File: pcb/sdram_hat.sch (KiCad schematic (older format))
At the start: 25 parts, among them J1 CONN_02X20, J2 CONN_02X20, J3 CONN_02X20, J4 CONN_02X20, J5 JACK_2P

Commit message: Some additional layout work on PCB
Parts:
- J1: footprint Pin_Headers:Pin_Header_Straight_2x21_Pitch2.54mm -> Socket_Strips:Socket_Strip_Straight_2x20_Pitch2.54mm
- J2, J3, J4: footprint Pin_Headers:Pin_Header_Straight_2x20_Pitch2.54mm -> Socket_Strips:Socket_Strip_Straight_2x20_Pitch2.54mm
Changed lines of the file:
@@
 F 0 "J2" H 1450 2700 50  0000 C CNN
 F 1 "CONN_02X20" V 1450 1650 50  0000 C CNN
-F 2 "Pin_Headers:Pin_Header_Straight_2x20_Pitch2.54mm" H 1450 700 50  0001 C CNN
+F 2 "Socket_Strips:Socket_Strip_Straight_2x20_Pitch2.54mm" H 1450 700 50  0001 C CNN
 F 3 "" H 1450 700 50  0001 C CNN
 	1    1450 1650
@@
 F 0 "J1" H 3350 2700 50  0000 C CNN
 F 1 "CONN_02X20" V 3350 1650 50  0000 C CNN
-F 2 "Pin_Headers:Pin_Header_Straight_2x21_Pitch2.54mm" H 3350 700 50  0001 C CNN
+F 2 "Socket_Strips:Socket_Strip_Straight_2x20_Pitch2.54mm" H 3350 700 50  0001 C CNN
 F 3 "" H 3350 700 50  0001 C CNN
 	1    3350 1650
@@
 F 0 "J3" H 5150 2700 50  0000 C CNN
 F 1 "CONN_02X20" V 5150 1650 50  0000 C CNN
-F 2 "Pin_Headers:Pin_Header_Straight_2x20_Pitch2.54mm" H 5150 700 50  0001 C CNN
+F 2 "Socket_Strips:Socket_Strip_Straight_2x20_Pitch2.54mm" H 5150 700 50  0001 C CNN
 F 3 "" H 5150 700 50  0001 C CNN
 	1    5150 1650
@@
 F 0 "J4" H 6900 2700 50  0000 C CNN
 F 1 "CONN_02X20" V 6900 1650 50  0000 C CNN
-F 2 "Pin_Headers:Pin_Header_Straight_2x20_Pitch2.54mm" H 6900 700 50  0001 C CNN
+F 2 "Socket_Strips:Socket_Strip_Straight_2x20_Pitch2.54mm" H 6900 700 50  0001 C CNN
 F 3 "" H 6900 700 50  0001 C CNN
 	1    6900 1650

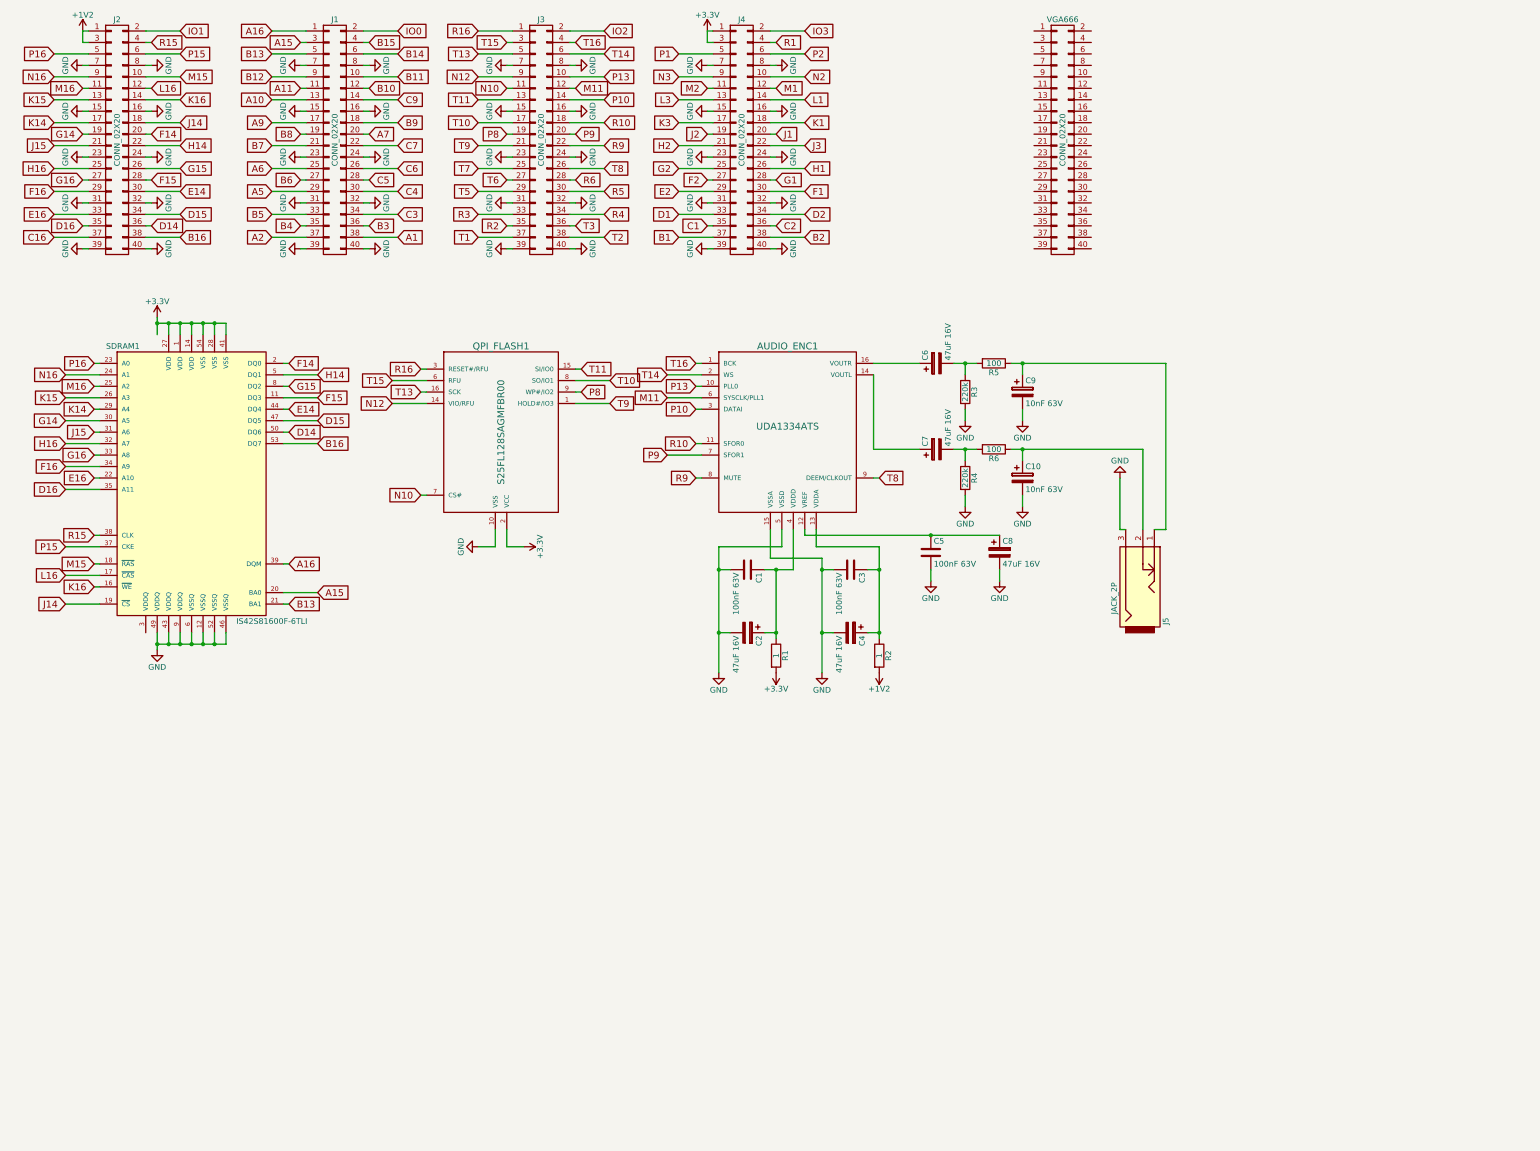
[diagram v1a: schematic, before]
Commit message: Added more pin definitions and progress on board layout
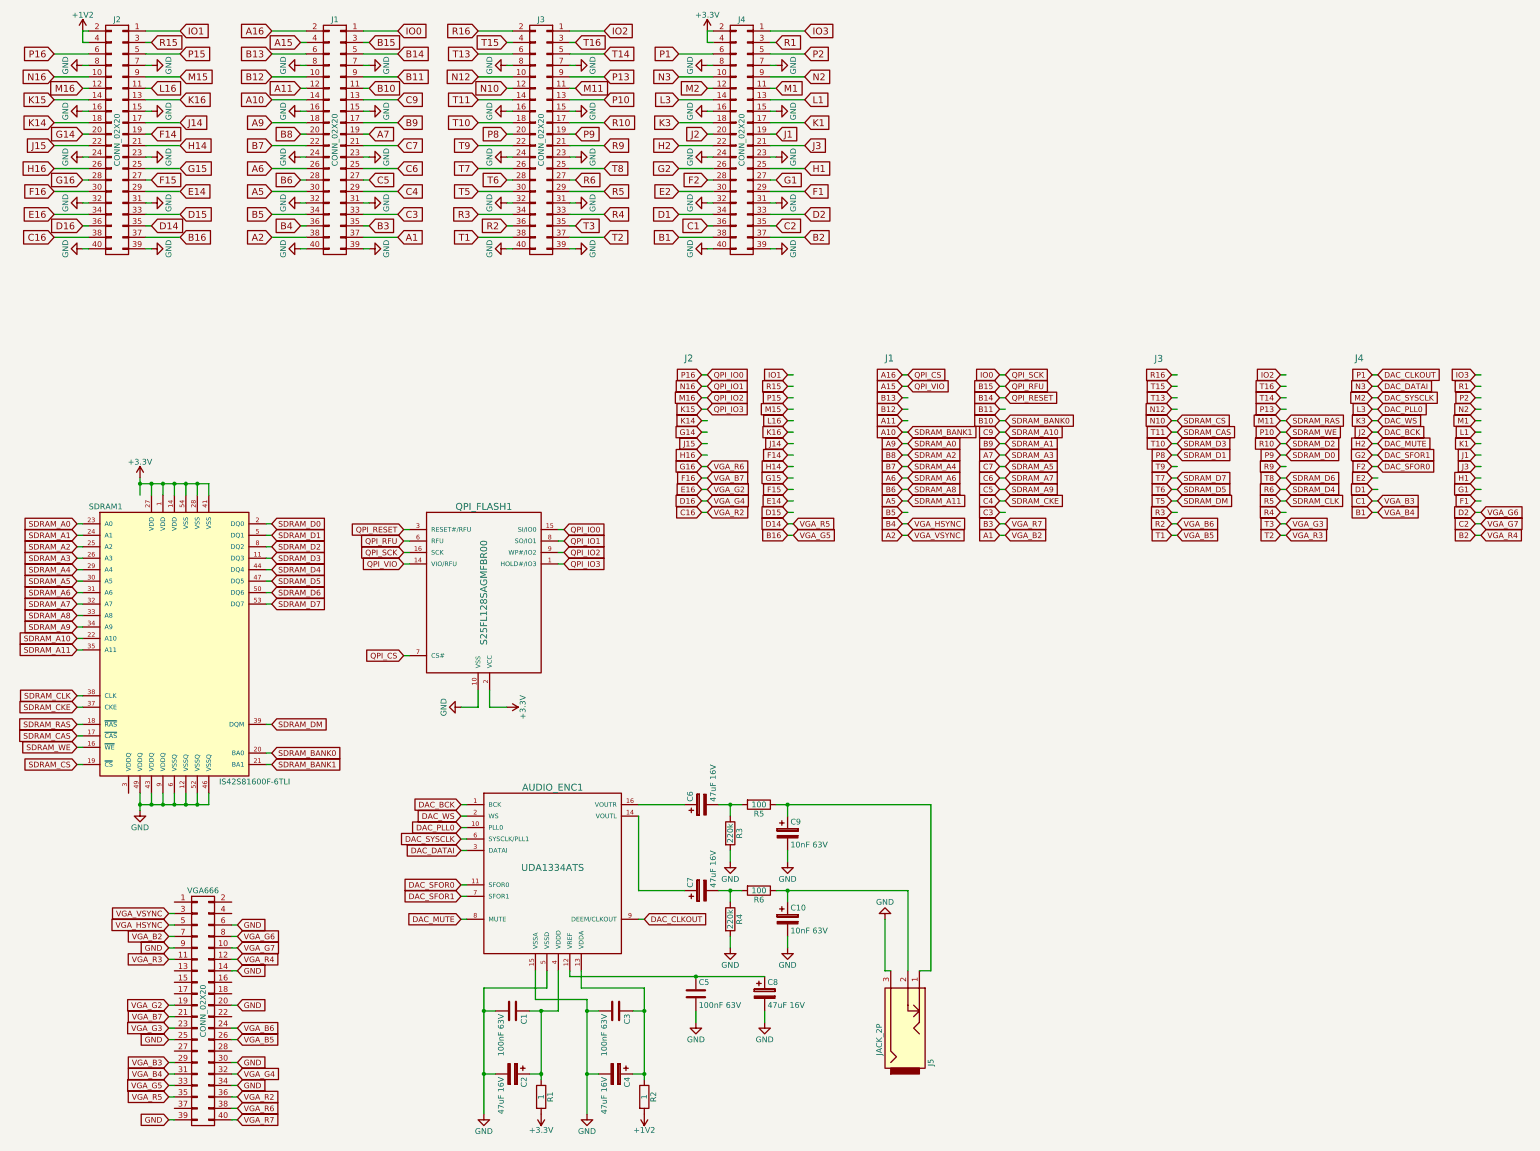
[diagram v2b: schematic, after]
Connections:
- net labels added: DAC_BCK, DAC_CLKOUT, DAC_DATAI, DAC_MUTE, DAC_PLL0, DAC_SFOR0, DAC_SFOR1, DAC_SYSCLK, DAC_WS, QPI_CS, QPI_IO0, QPI_IO1, QPI_IO2, QPI_IO3, QPI_RESET, QPI_RFU, QPI_SCK, QPI_VIO, SDRAM_A0, SDRAM_A1, SDRAM_A10, SDRAM_A11, SDRAM_A2, SDRAM_A3, SDRAM_A4, SDRAM_A5, SDRAM_A6, SDRAM_A7, SDRAM_A8, SDRAM_A9, SDRAM_BANK0, SDRAM_BANK1, SDRAM_CAS, SDRAM_CKE, SDRAM_CLK, SDRAM_CS, SDRAM_D0, SDRAM_D1, SDRAM_D2, SDRAM_D3, SDRAM_D4, SDRAM_D5, SDRAM_D6, SDRAM_D7, SDRAM_DM, SDRAM_RAS, SDRAM_WE, VGA_B2, VGA_B3, VGA_B4, VGA_B5, VGA_B6, VGA_B7, VGA_G2, VGA_G3, VGA_G4, VGA_G5, VGA_G6, VGA_G7, VGA_HSYNC, VGA_R2, VGA_R3, VGA_R4, VGA_R5, VGA_R6, VGA_R7, VGA_VSYNC
- wire segments 272 -> 416
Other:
- note added: "J1\n"
- note added: "J2\n"
- note added: "J3\n\n"
- note added: "J4\n"
- moved on the sheet: AUDIO_ENC1, C1, C10, C2, C3, C4, C5, C6, C7, C8, C9, J5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

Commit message: Added TH passives, analog+digital ground planes, some autorouting stuff.
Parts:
- removed C10, C9: 10nF 63V, Capacitors_SMD:CP_Elec_3x5.3, symbol CP
- removed J5: JACK_2P, Connectors:BARREL_JACK, symbol JACK_2P
- added C10, C9: 10nF, Capacitors_THT:C_Disc_D4.3mm_W1.9mm_P5.00mm, symbol C
- added J5: AUDIO_OUT_JACK, pcb:SJ1-352XNG, symbol CONN_01X05
- added R7: 0, symbol R
- AUDIO_ENC1: footprint SMD_Packages:SSOP-20 -> Housings_SSOP:SSOP-16_4.4x5.2mm_Pitch0.65mm
- C1, C3, C5: footprint Capacitors_SMD:C_0201 -> Capacitors_THT:C_Disc_D4.3mm_W1.9mm_P5.00mm
- C2, C4, C6, C7, C8: footprint Capacitors_SMD:CP_Elec_3x5.3 -> Capacitors_THT:CP_Radial_D5.0mm_P2.50mm
- R1, R2, R3, R4, R5, R6: footprint Resistors_SMD:R_0201 -> Resistors_THT:R_Axial_DIN0207_L6.3mm_D2.5mm_P10.16mm_Horizontal
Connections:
- net labels added: GNDA
- wire segments 416 -> 420
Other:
- moved on the sheet: VGA666

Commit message: Fixing AGND on a few DAC components
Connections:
- wire segments 420 -> 421
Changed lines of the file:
@@
 Wire Wire Line
 	7300 7550 7300 7450
-$Comp
-L GND #PWR047
-U 1 1 59A08245
-P 6800 7950
-F 0 "#PWR047" H 6800 7700 50  0001 C CNN
-F 1 "GND" H 6800 7800 50  0000 C CNN
-F 2 "" H 6800 7950 50  0001 C CNN
-F 3 "" H 6800 7950 50  0001 C CNN
-	1    6800 7950
-	1    0    0    -1
-$EndComp
-$Comp
-L GND #PWR048
-U 1 1 59A08273
-P 7300 7950
-F 0 "#PWR048" H 7300 7700 50  0001 C CNN
-F 1 "GND" H 7300 7800 50  0000 C CNN
-F 2 "" H 7300 7950 50  0001 C CNN
-F 3 "" H 7300 7950 50  0001 C CNN
-	1    7300 7950
-	1    0    0    -1
-$EndComp
 Wire Wire Line
 	6800 7850 6800 7950
@@
 Wire Wire Line
 	7300 8300 7300 8200
-$Comp
-L GND #PWR049
-U 1 1 59A08825
-P 6800 8700
-F 0 "#PWR049" H 6800 8450 50  0001 C CNN
-F 1 "GND" H 6800 8550 50  0000 C CNN
-F 2 "" H 6800 8700 50  0001 C CNN
-F 3 "" H 6800 8700 50  0001 C CNN
-	1    6800 8700
-	1    0    0    -1
-$EndComp
-$Comp
-L GND #PWR050
-U 1 1 59A0882B
-P 7300 8700
-F 0 "#PWR050" H 7300 8450 50  0001 C CNN
-F 1 "GND" H 7300 8550 50  0000 C CNN
-F 2 "" H 7300 8700 50  0001 C CNN
-F 3 "" H 7300 8700 50  0001 C CNN
-	1    7300 8700
-	1    0    0    -1
-$EndComp
 Wire Wire Line
 	6800 8600 6800 8700
@@
 Connection ~ 5150 9800
 $Comp
-L +3.3V #PWR051
+L +3.3V #PWR047
 U 1 1 59A09CD5
 P 5150 10200
-F 0 "#PWR051" H 5150 10050 50  0001 C CNN
+F 0 "#PWR047" H 5150 10050 50  0001 C CNN
 F 1 "+3.3V" H 5150 10340 50  0000 C CNN
 F 2 "" H 5150 10200 50  0001 C CNN
@@
 Connection ~ 6050 9800
 $Comp
-L +1V2 #PWR052
+L +1V2 #PWR048
 U 1 1 59A0A16B
 P 6050 10200
-F 0 "#PWR052" H 6050 10050 50  0001 C CNN
+F 0 "#PWR048" H 6050 10050 50  0001 C CNN
 F 1 "+1V2" H 6050 10340 50  0000 C CNN
 F 2 "" H 6050 10200 50  0001 C CNN
@@
 	8450 8200 8450 9100
 Wire Wire Line
-	8550 8450 8550 9100
+	8550 9000 8550 9100
 Text GLabel 9700 5800 0    49   Input ~ 0
 VGA_VSYNC
@@
 SDRAM_A1
 $Comp
-L GNDA #PWR053
-U 1 1 59A5A27F
-P 4650 10150
-F 0 "#PWR053" H 4650 9900 50  0001 C CNN
-F 1 "GNDA" H 4650 10000 50  0000 C CNN
-F 2 "" H 4650 10150 50  0001 C CNN
-F 3 "" H 4650 10150 50  0001 C CNN
-	1    4650 10150
-	1    0    0    -1
-$EndComp
-$Comp
-L GNDA #PWR054
+L GNDA #PWR050
 U 1 1 59A5A3F1
 P 5550 10150
-F 0 "#PWR054" H 5550 9900 50  0001 C CNN
+F 0 "#PWR050" H 5550 9900 50  0001 C CNN
 F 1 "GNDA" H 5550 10000 50  0000 C CNN
 F 2 "" H 5550 10150 50  0001 C CNN
@@
 $EndComp
 $Comp
-L GNDA #PWR055
+L GNDA #PWR051
 U 1 1 59A5A447
 P 6500 9350
-F 0 "#PWR055" H 6500 9100 50  0001 C CNN
+F 0 "#PWR051" H 6500 9100 50  0001 C CNN
 F 1 "GNDA" H 6500 9200 50  0000 C CNN
 F 2 "" H 6500 9350 50  0001 C CNN
@@
 $EndComp
 $Comp
-L GNDA #PWR056
+L GNDA #PWR052
 U 1 1 59A5A49D
 P 7100 9350
-F 0 "#PWR056" H 7100 9100 50  0001 C CNN
+F 0 "#PWR052" H 7100 9100 50  0001 C CNN
 F 1 "GNDA" H 7100 9200 50  0000 C CNN
 F 2 "" H 7100 9350 50  0001 C CNN
@@
 $EndComp
 $Comp
-L GNDA #PWR057
+L GNDA #PWR053
 U 1 1 59A5A4F3
-P 8550 8450
-F 0 "#PWR057" H 8550 8200 50  0001 C CNN
-F 1 "GNDA" H 8550 8300 50  0000 C CNN
-F 2 "" H 8550 8450 50  0001 C CNN
-F 3 "" H 8550 8450 50  0001 C CNN
-	1    8550 8450
-	-1   0    0    1
-$EndComp
-$Comp
-L GNDA #PWR058
+P 8900 9000
+F 0 "#PWR053" H 8900 8750 50  0001 C CNN
+F 1 "GNDA" H 8900 8850 50  0000 C CNN
+F 2 "" H 8900 9000 50  0001 C CNN
+F 3 "" H 8900 9000 50  0001 C CNN
+	1    8900 9000
+	0    -1   -1   0
+$EndComp
+$Comp
+L GNDA #PWR054
 U 1 1 59A5B04F
 P 1700 9450
-F 0 "#PWR058" H 1700 9200 50  0001 C CNN
+F 0 "#PWR054" H 1700 9200 50  0001 C CNN
 F 1 "GNDA" H 1700 9300 50  0000 C CNN
 F 2 "" H 1700 9450 50  0001 C CNN
@@
 $EndComp
 $Comp
-L GND #PWR059
+L GND #PWR055
 U 1 1 59A5B0A5
 P 2200 9450
-F 0 "#PWR059" H 2200 9200 50  0001 C CNN
+F 0 "#PWR055" H 2200 9200 50  0001 C CNN
 F 1 "GND" H 2200 9300 50  0000 C CNN
 F 2 "" H 2200 9450 50  0001 C CNN
@@
 Wire Wire Line
 	1700 9350 1700 9450
+$Comp
+L GNDA #PWR056
+U 1 1 59A26E0F
+P 6800 7950
+F 0 "#PWR056" H 6800 7700 50  0001 C CNN
+F 1 "GNDA" H 6800 7800 50  0000 C CNN
+F 2 "" H 6800 7950 50  0001 C CNN
+F 3 "" H 6800 7950 50  0001 C CNN
+	1    6800 7950
+	1    0    0    -1
+$EndComp
+$Comp
+L GNDA #PWR057
+U 1 1 59A26E68
+P 7300 7950
+F 0 "#PWR057" H 7300 7700 50  0001 C CNN
+F 1 "GNDA" H 7300 7800 50  0000 C CNN
+F 2 "" H 7300 7950 50  0001 C CNN
+F 3 "" H 7300 7950 50  0001 C CNN
+	1    7300 7950
+	1    0    0    -1
+$EndComp
+$Comp
+L GNDA #PWR058
+U 1 1 59A26EC1
+P 7300 8700
+F 0 "#PWR058" H 7300 8450 50  0001 C CNN
+F 1 "GNDA" H 7300 8550 50  0000 C CNN
+F 2 "" H 7300 8700 50  0001 C CNN
+F 3 "" H 7300 8700 50  0001 C CNN
+	1    7300 8700
+	1    0    0    -1
+$EndComp
+$Comp
+L GNDA #PWR059
+U 1 1 59A26F1A
+P 6800 8700
+F 0 "#PWR059" H 6800 8450 50  0001 C CNN
+F 1 "GNDA" H 6800 8550 50  0000 C CNN
+F 2 "" H 6800 8700 50  0001 C CNN
+F 3 "" H 6800 8700 50  0001 C CNN
+	1    6800 8700
+	1    0    0    -1
+$EndComp
+Wire Wire Line
+	8550 9000 8900 9000
+$Comp
+L GND #PWR?
+U 1 1 59A277DD
+P 4650 10150
+F 0 "#PWR?" H 4650 9900 50  0001 C CNN
+F 1 "GND" H 4650 10000 50  0000 C CNN
+F 2 "" H 4650 10150 50  0001 C CNN
+F 3 "" H 4650 10150 50  0001 C CNN
+	1    4650 10150
+	1    0    0    -1
+$EndComp
 $EndSCHEMATC

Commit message: Moved to SMD, moving components to back side, added some decoupling
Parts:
- added C11, C12, C13: 100nF, Capacitors_SMD:C_0805_HandSoldering, symbol C_Small
- C1, C10, C3, C5, C9: footprint Capacitors_THT:C_Disc_D4.3mm_W1.9mm_P5.00mm -> Capacitors_SMD:C_0805_HandSoldering
- R1, R2, R3, R4, R5, R6: footprint Resistors_THT:R_Axial_DIN0207_L6.3mm_D2.5mm_P10.16mm_Horizontal -> Resistors_SMD:R_0805_HandSoldering
- R7: footprint (none) -> Resistors_SMD:R_0805_HandSoldering
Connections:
- wire segments 421 -> 429

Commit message: Switch out larger footprints, minor pinout tweaks
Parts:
- AUDIO_ENC1: footprint Housings_SSOP:SSOP-16_4.4x5.2mm_Pitch0.65mm -> pcb:SSOP-16_4.4x5.2mm_Pitch0.65mm_ExtendedPad
- QPI_FLASH1: footprint Housings_SOIC:SOIC-16_3.9x9.9mm_Pitch1.27mm -> pcb:SOIC-16_3.9x9.9mm_Pitch1.27mm_ExtendedPad
- SDRAM1: footprint pcb:TSOPII-54_10.16x22.22mm-Pitch0.8mm -> pcb:TSOPII-54_10.16x22.22mm_Pitch0.8mm_ExtendedPad
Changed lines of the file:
@@
 F 0 "SDRAM1" H 1350 7250 50  0000 C CNN
 F 1 "IS42S81600F-6TLI" H 2650 4850 50  0000 C CNN
-F 2 "pcb:TSOPII-54_10.16x22.22mm-Pitch0.8mm" H 1950 6050 50  0001 C CIN
+F 2 "pcb:TSOPII-54_10.16x22.22mm_Pitch0.8mm_ExtendedPad" H 1950 6050 50  0001 C CIN
 F 3 "" H 1950 5800 50  0001 C CNN
 	1    1950 6050
@@
 F 0 "QPI_FLASH1" H 4650 6350 60  0000 C CNN
 F 1 "S25FL128SAGMFBR00" V 4650 5600 60  0000 C CNN
-F 2 "Housings_SOIC:SOIC-16_3.9x9.9mm_Pitch1.27mm" H 4650 4850 60  0001 C CNN
+F 2 "pcb:SOIC-16_3.9x9.9mm_Pitch1.27mm_ExtendedPad" H 4650 4850 60  0001 C CNN
 F 3 "" H 4650 4850 60  0001 C CNN
 	1    4650 5600
@@
 F 0 "AUDIO_ENC1" H 5250 8800 60  0000 C CNN
 F 1 "UDA1334ATS" H 5250 8100 60  0000 C CNN
-F 2 "Housings_SSOP:SSOP-16_4.4x5.2mm_Pitch0.65mm" H 5250 8050 60  0001 C CNN
+F 2 "pcb:SSOP-16_4.4x5.2mm_Pitch0.65mm_ExtendedPad" H 5250 8050 60  0001 C CNN
 F 3 "" H 5250 8050 60  0001 C CNN
 	1    5250 8050
@@
 Text GLabel 6600 4800 2    49   Input ~ 0
 VGA_VSYNC
-Text GLabel 6600 4900 2    49   Input ~ 0
+Text GLabel 7350 5100 2    49   Input ~ 0
 VGA_HSYNC
 Text GLabel 9200 5100 2    49   Input ~ 0
@@
 Text GLabel 7350 5000 2    49   Input ~ 0
 VGA_G6
-Text GLabel 7350 5100 2    49   Input ~ 0
+Text GLabel 6600 4900 2    49   Input ~ 0
 VGA_G7
 Text GLabel 8350 5000 2    49   Input ~ 0
@@
 Text GLabel 9200 3900 2    49   Input ~ 0
 QPI_RFU
-Text GLabel 9200 3800 2    49   Input ~ 0
+Text GLabel 6600 4000 2    49   Input ~ 0
 QPI_SCK
 Text GLabel 8350 4000 2    49   Input ~ 0
@@
 Text GLabel 6600 3900 2    49   Input ~ 0
 QPI_IO0
-Text GLabel 6600 4000 2    49   Input ~ 0
+Text GLabel 8350 3700 2    49   Input ~ 0
 QPI_IO1
 Text GLabel 7350 3900 2    49   Input ~ 0
